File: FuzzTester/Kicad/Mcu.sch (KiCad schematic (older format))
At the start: 11 parts, among them J7 Boot Reset PinHeader, J8 SPI Test PinHeader, J9 SWD_PinHeader, U3 STM32F103C8Tx, Y1 8MHz

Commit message: PCB fixes
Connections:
- wire segments 55 -> 54
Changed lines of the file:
@@
 encoding utf-8
 Sheet 3 10
-Title ""
+Title "Guitar Pedal Effect Fuzz Digitally Controlled"
 Date ""
-Rev ""
+Rev "0.1"
 Comp ""
 Comment1 ""
@@
 Wire Wire Line
 	3400 2100 3400 2200
-Wire Wire Line
-	3400 2100 3500 2100
 $EndSCHEMATC

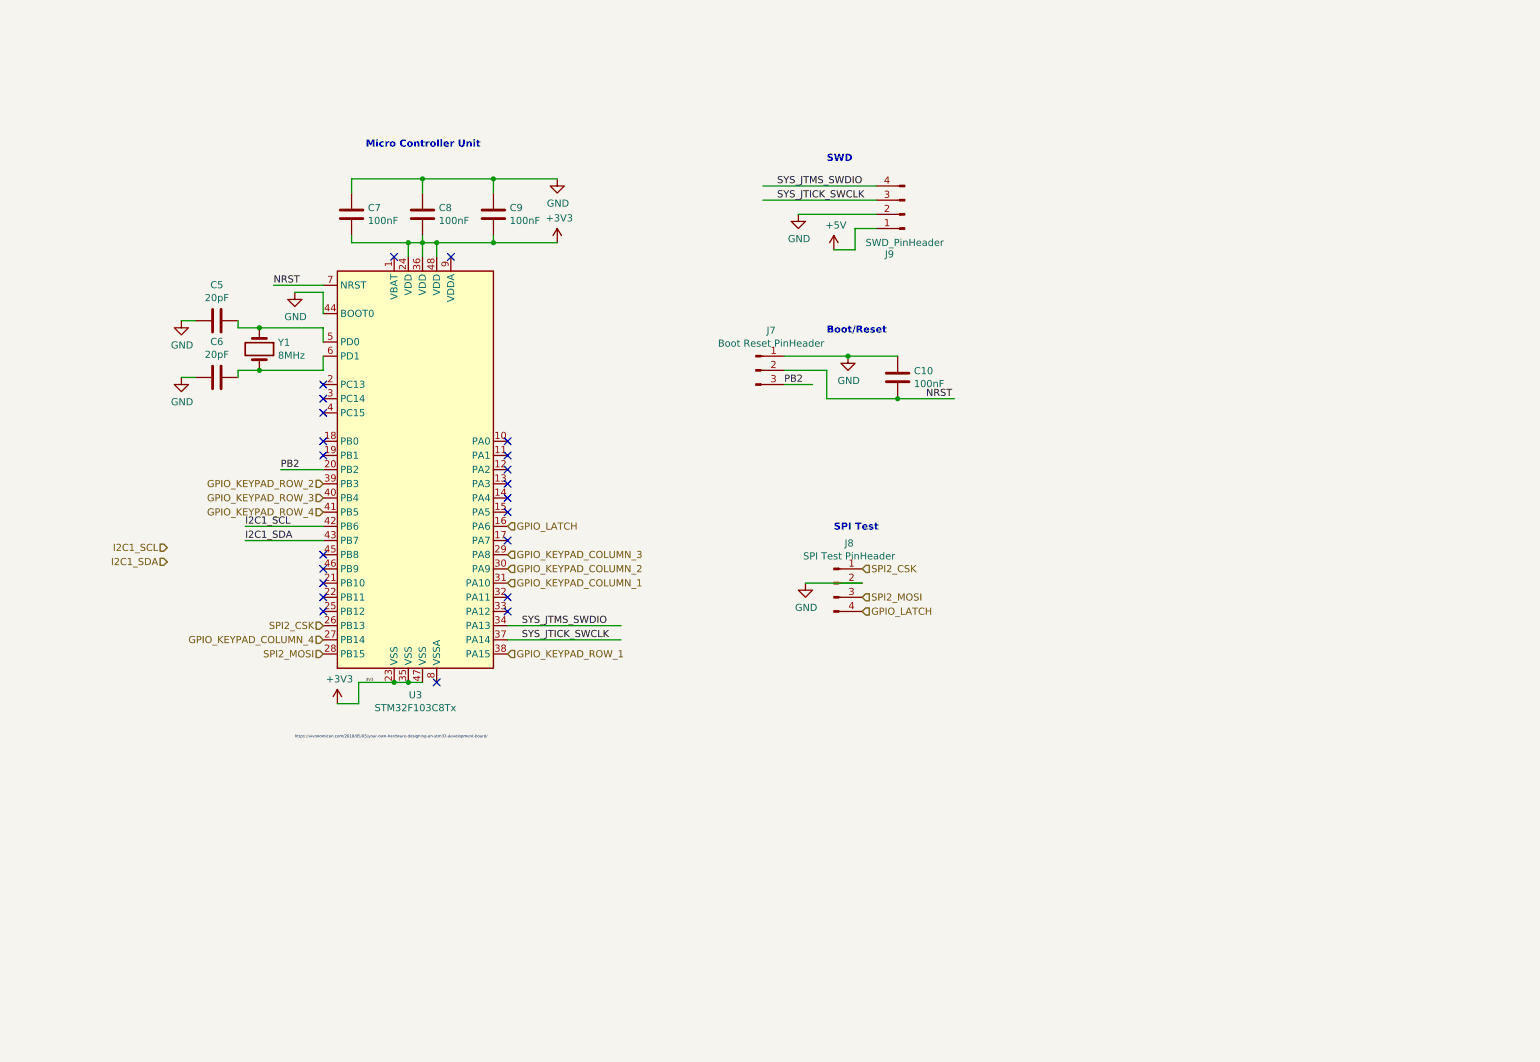
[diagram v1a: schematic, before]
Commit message: Schematics UI/MCU -> MCU + PCB improvements
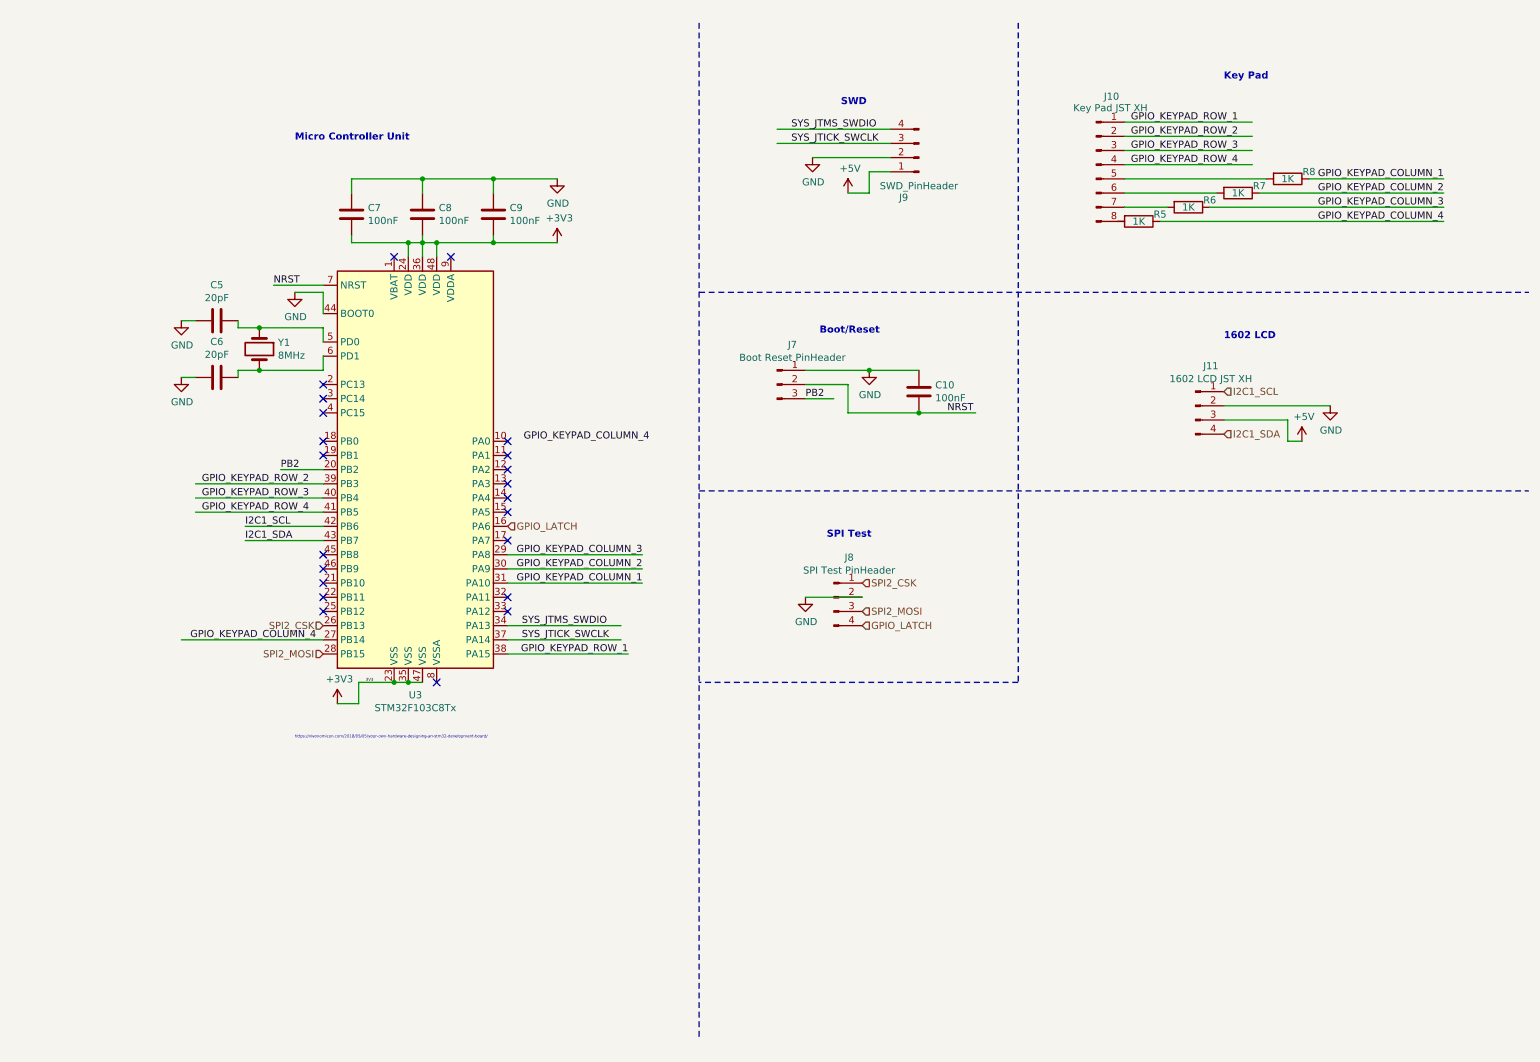
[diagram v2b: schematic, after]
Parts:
- added J10: Key Pad JST XH, Connector_JST:JST_XH_B8B-XH-A_1x08_P2.50mm_Vertical, symbol Connector:Conn_01x08_Male
- added J11: 1602 LCD JST XH, Connector_JST:JST_XH_B4B-XH-A_1x04_P2.50mm_Vertical, symbol Connector:Conn_01x04_Male
- added R5, R6, R7, R8: 1K, Resistor_SMD:R_0805_2012Metric_Pad1.15x1.40mm_HandSolder, symbol Device:R
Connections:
- wire segments 54 -> 77
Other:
- note added: "1602 LCD\n\n\n"
- note added: "Key Pad\n\n\n\n"
- moved on the sheet: C10, J7, J8, J9

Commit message: PCB Placement 100x82
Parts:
- removed J11: 1602 LCD JST XH, Connector_JST:JST_XH_B4B-XH-A_1x04_P2.50mm_Vertical, symbol Connector:Conn_01x04_Male
- added J11: LCD JST XH, Connector_JST:JST_XH_B6B-XH-A_1x06_P2.50mm_Vertical, symbol Connector:Conn_01x06_Male
- added J12: Bypass Switch JST XH, Connector_JST:JST_XH_B2B-XH-A_1x02_P2.50mm_Vertical, symbol Connector:Conn_01x02_Male
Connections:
- net labels added: 1602_BACK_LIGHT_PIN_1, 1602_BACK_LIGHT_PIN_2, BYPASS_MODE_3V3, BYPASS_SWITCH_3V3
- wire segments 77 -> 81
- no-connect marks 22 -> 20
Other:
- note added: "Bypass\n\n\n"
- note added: "Pull Down Resistor"
- moved on the sheet: R5, R6, R7, R8

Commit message: Starting to route
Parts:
- added RN1, RN2: R_Pack04, Resistor_SMD:R_Array_Convex_4x0603, symbol Device:R_Pack04
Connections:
- net labels added: GPIO_LATCH_MCU, I2C1_SCL_MCU, I2C1_SDA_MCU, SPI2_CSK_MCU, SPI2_MOSI_MCU, SYS_JTICK_SWCLK_MCU, SYS_JTMS_SWDIO_MCU
- wire segments 81 -> 93
- no-connect marks 20 -> 22
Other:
- note added: "Check: Concave or Convex footprint"
- note added: "I2C CROSSTALK\n\n\n"
- note added: "SWDIO/I2C CROSSTALK\n\n\n"
- moved on the sheet: C5, C6, C7, C8, C9, U3, Y1
